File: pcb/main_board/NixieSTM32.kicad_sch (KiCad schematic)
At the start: 36 parts, among them J1 Conn_ARM_SWD_6, Q1 FQU11P06TU, SW1 SW_SPDT, U1 STM32L010K4T6, U2 MAX6817, U3 TPS7A05SOT23, U4 LT3470ITS8PBF, Y1 32.768kHz

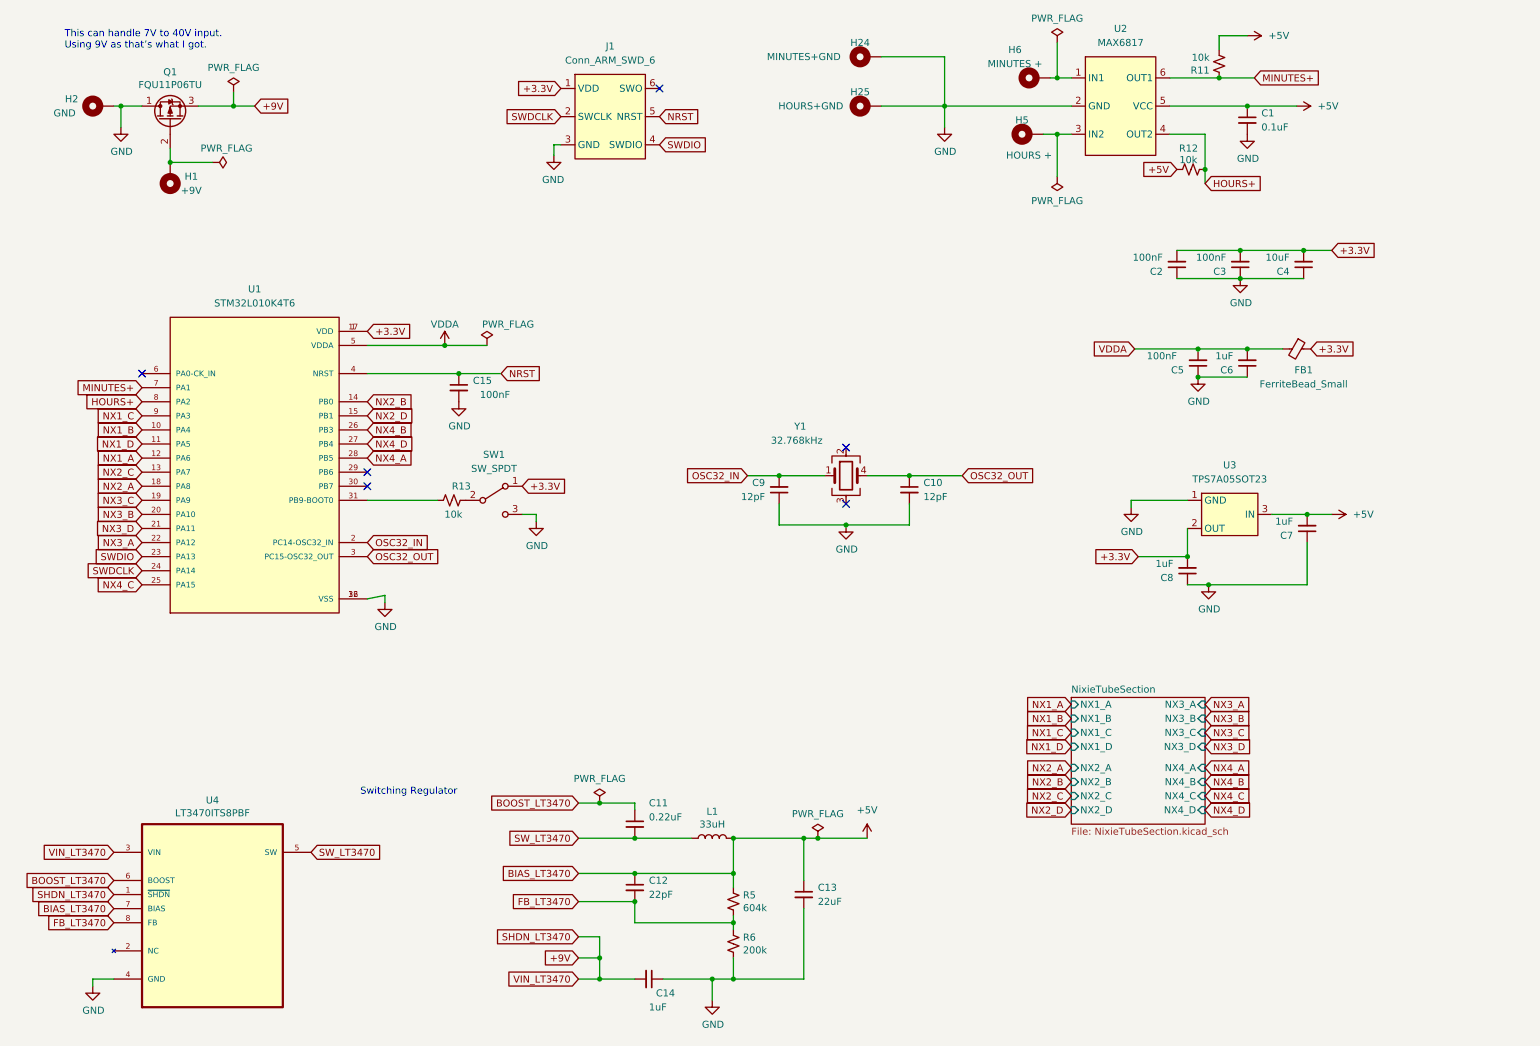
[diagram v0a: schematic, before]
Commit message: Adjusting README, removing 3mf files, adding both v1 and v1 step files.
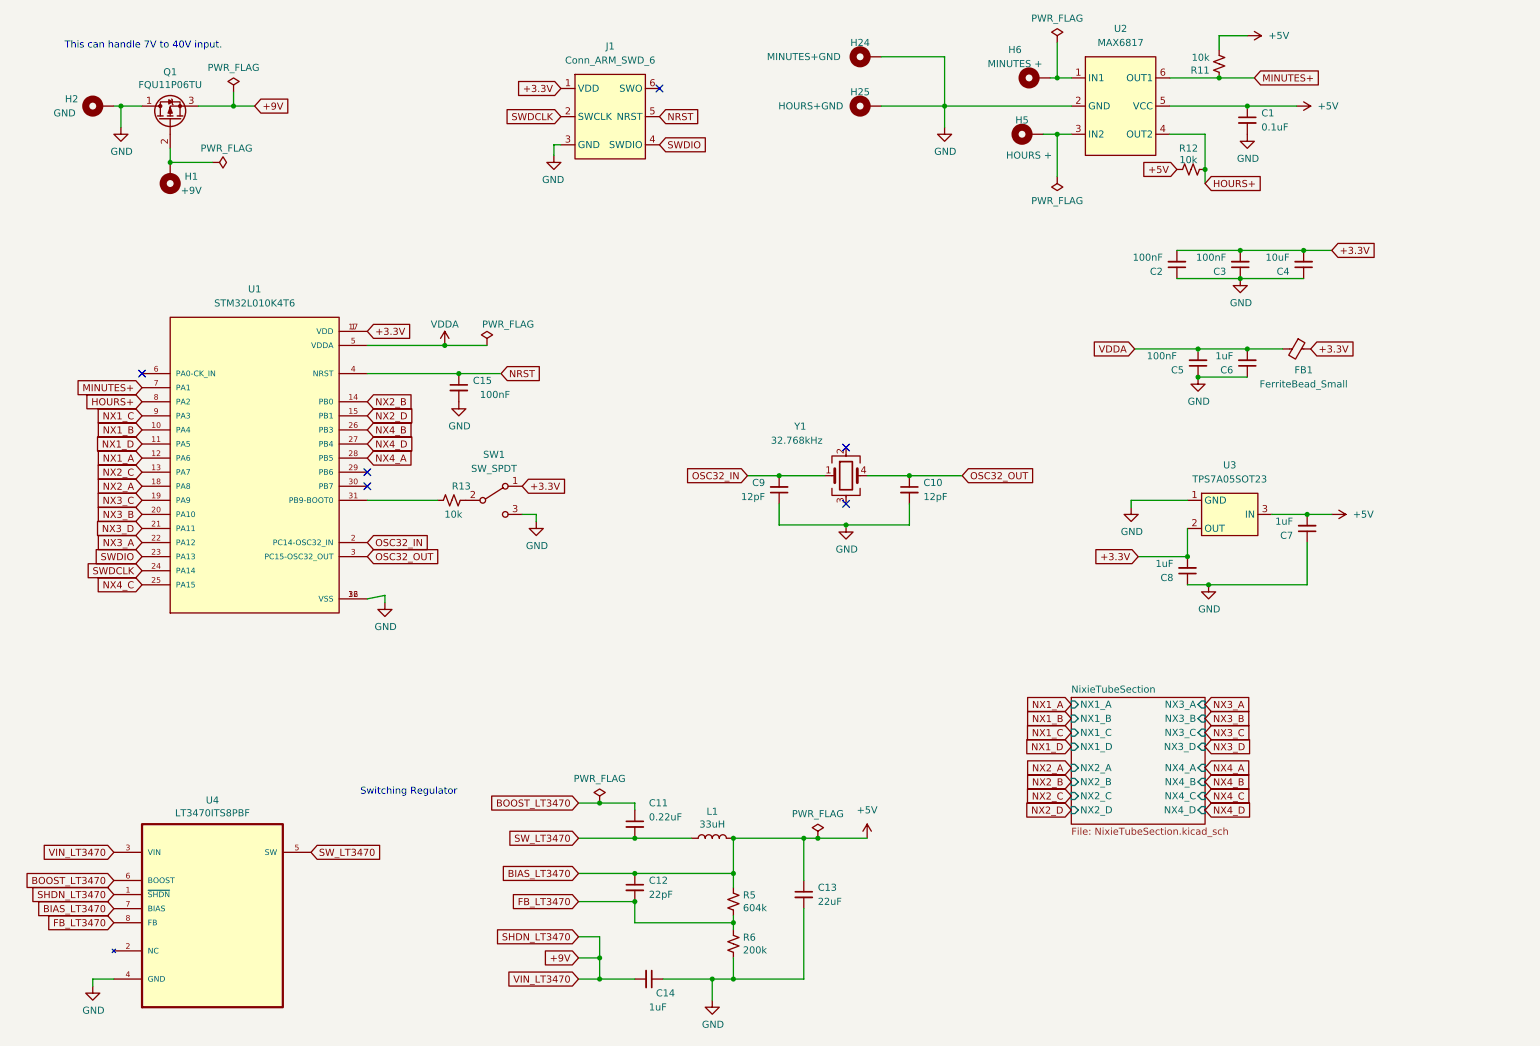
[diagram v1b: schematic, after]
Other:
- note added: "This can handle 7V to 40V input."
- note removed: "This can handle 7V to 40V input. Using 9V as that’s what I got."

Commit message: Adding images and updating README.
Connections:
- net VDDA: no longer names the net of C5.2, C6.2, FB1.2, U1.5 (VDDA)
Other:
- note added: "Debounce"
- note added: "Nixie Clock"
- note added: "Reverse Polarity Protection"
- note added: "STM32"
- note added: "Tag Connect"
- note added: "Voltage Regulator"
- moved on the sheet: C1, C10, C11, C12, C13, C14, C15, C2, C3, C4, C5, C6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
